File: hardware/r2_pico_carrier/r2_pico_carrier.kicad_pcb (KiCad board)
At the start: 2 copper layers, 80 x 90 mm, 67 parts, among them J1 5V in, J2 OLED socket, SW1 display, U1 PCA9517A

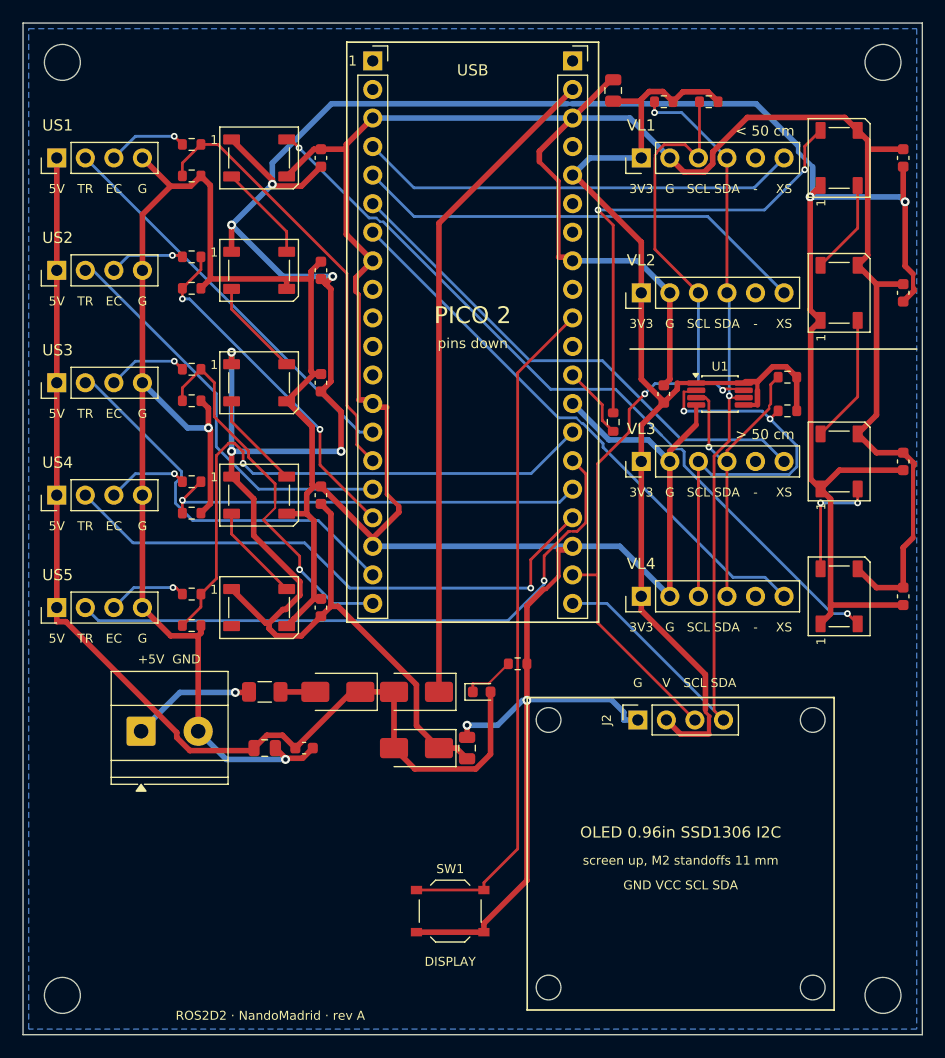
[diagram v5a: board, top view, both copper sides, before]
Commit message: Carrier board: plain 0603 status LEDs, one GPIO each (VL1-4 = GP28/27/22/9, US1-5 = GP0/1/6-8), in place of the WS2812B chain; no VLED rail; BOM 17 lines
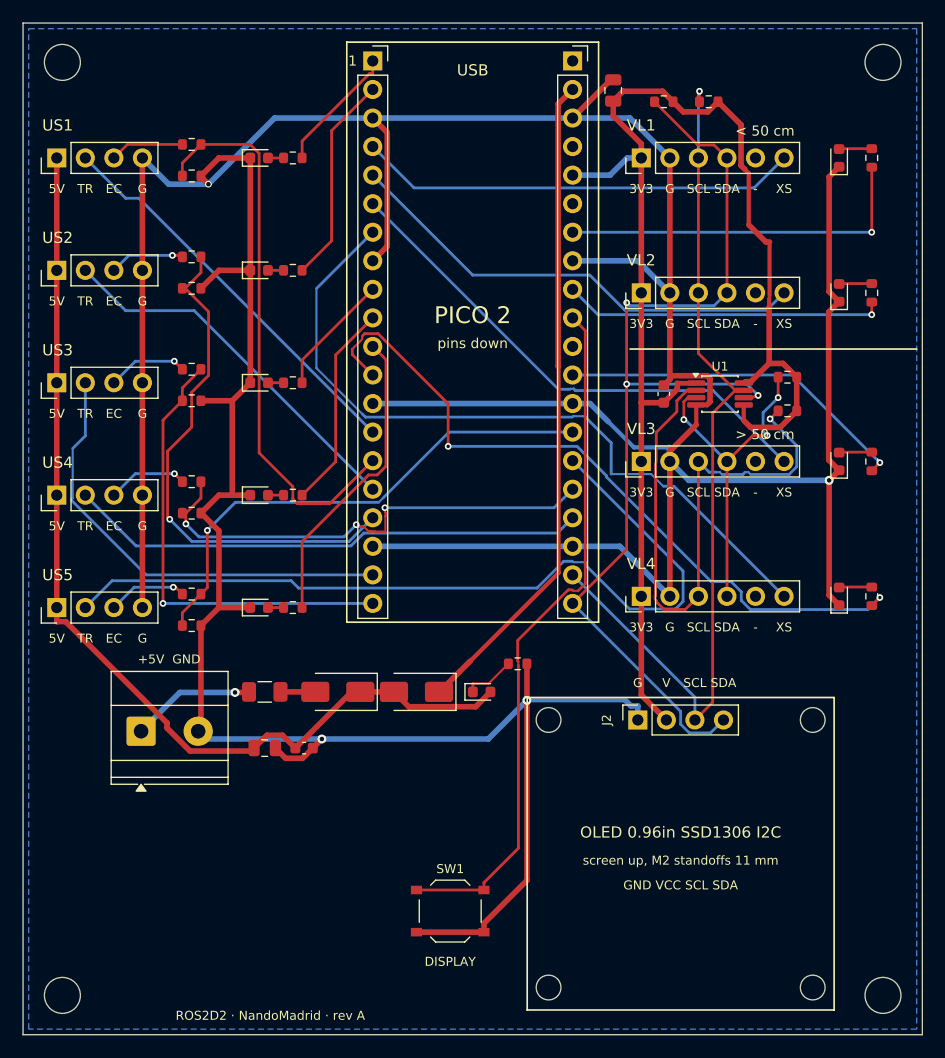
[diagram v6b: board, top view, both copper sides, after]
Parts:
- removed C11, C12, C13, C14, C15, C16, C17, C18, C19: 100n, Capacitor_SMD:C_0603_1608Metric
- removed C3: 10u, Capacitor_SMD:C_0805_2012Metric
- removed D3: SS34, Diode_SMD:D_SMA
- removed R6: 33, Resistor_SMD:R_0603_1608Metric
- added R31: 1k, Resistor_SMD:R_0603_1608Metric, F.Cu at (75.5, 12.0)
- added R32: 1k, Resistor_SMD:R_0603_1608Metric, F.Cu at (75.5, 24.0)
- added R33: 1k, Resistor_SMD:R_0603_1608Metric, F.Cu at (75.5, 39.0)
- added R34: 1k, Resistor_SMD:R_0603_1608Metric, F.Cu at (75.5, 51.0)
- added R35: 1k, Resistor_SMD:R_0603_1608Metric, F.Cu at (24.0, 12.0)
- added R36: 1k, Resistor_SMD:R_0603_1608Metric, F.Cu at (24.0, 22.0)
- added R37: 1k, Resistor_SMD:R_0603_1608Metric, F.Cu at (24.0, 32.0)
- added R38: 1k, Resistor_SMD:R_0603_1608Metric, F.Cu at (24.0, 42.0)
- added R39: 1k, Resistor_SMD:R_0603_1608Metric, F.Cu at (24.0, 52.0)
- LED1, LED2, LED3, LED4, LED5, LED6, LED7, LED8, LED9: value WS2812B -> red; footprint LED_SMD:LED_WS2812B_PLCC4_5.0x5.0mm_P3.2mm -> LED_SMD:LED_0603_1608Metric
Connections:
- JP1 pad 1: unconnected-(JP1-Pin_1-Pad1) -> STAT5
- JP1 pad 10: unconnected-(JP1-Pin_10-Pad10) -> STAT8
- JP1 pad 11: unconnected-(JP1-Pin_11-Pad11) -> STAT9
- JP1 pad 12: unconnected-(JP1-Pin_12-Pad12) -> STAT4
- JP1 pad 2: unconnected-(JP1-Pin_2-Pad2) -> STAT6
- JP1 pad 9: unconnected-(JP1-Pin_9-Pad9) -> STAT7
- JP2 pad 12: LED_DIN_P -> STAT3
- JP2 pad 7: unconnected-(JP2-Pin_7-Pad7) -> STAT1
- JP2 pad 9: unconnected-(JP2-Pin_9-Pad9) -> STAT2
- LED1 pad 1: VLED -> GND
- LED1 pad 2: LED_D1 -> STAT1_A
- LED2 pad 1: VLED -> GND
- LED2 pad 2: LED_D2 -> STAT2_A
- LED3 pad 1: VLED -> GND
- LED3 pad 2: LED_D3 -> STAT3_A
- LED4 pad 1: VLED -> GND
- LED4 pad 2: LED_D4 -> STAT4_A
- LED5 pad 1: VLED -> GND
- LED5 pad 2: LED_D5 -> STAT5_A
- LED6 pad 1: VLED -> GND
- LED6 pad 2: LED_D6 -> STAT6_A
- LED7 pad 1: VLED -> GND
- LED7 pad 2: LED_D7 -> STAT7_A
- LED8 pad 1: VLED -> GND
- LED8 pad 2: LED_D8 -> STAT8_A
- LED9 pad 1: VLED -> GND
- LED9 pad 2: unconnected-(LED9-DOUT-Pad2) -> STAT9_A
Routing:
- net VLED: track 261.3 -> 0.00 mm, vias 8 -> 0
- net LED_D4: track 69.4 -> 0.00 mm, vias 2 -> 0
- net STAT4: track 0.00 -> 65.1 mm, vias 0 -> 2
- net LED_DIN: track 42.6 -> 0.00 mm, vias 2 -> 0
- net GND: track 473.4 -> 431.8 mm
- net STAT1: track 0.00 -> 32.4 mm, vias 0 -> 1
- net STAT3: track 0.00 -> 31.6 mm, vias 0 -> 1
- net STAT2: track 0.00 -> 28.7 mm, vias 0 -> 1
- net STAT9: track 0.00 -> 27.3 mm
- net STAT6: track 0.00 -> 18.7 mm
- net STAT8: track 0.00 -> 18.4 mm
- net +3V3: track 103.7 -> 121.8 mm
- net TRIG5: track 56.1 -> 74.2 mm, vias 1 -> 0
- net XSHUT4: track 50.2 -> 65.9 mm
- net ECHO2_P: track 31.3 -> 46.4 mm, vias 2 -> 1
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
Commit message: Carrier board: USB-C power input (5.1k on CC, own SS34, shared fuse), Qwiic + 6-pin expansion header (I2C, 5V, 3V3, RUN), Astromech logo on the front
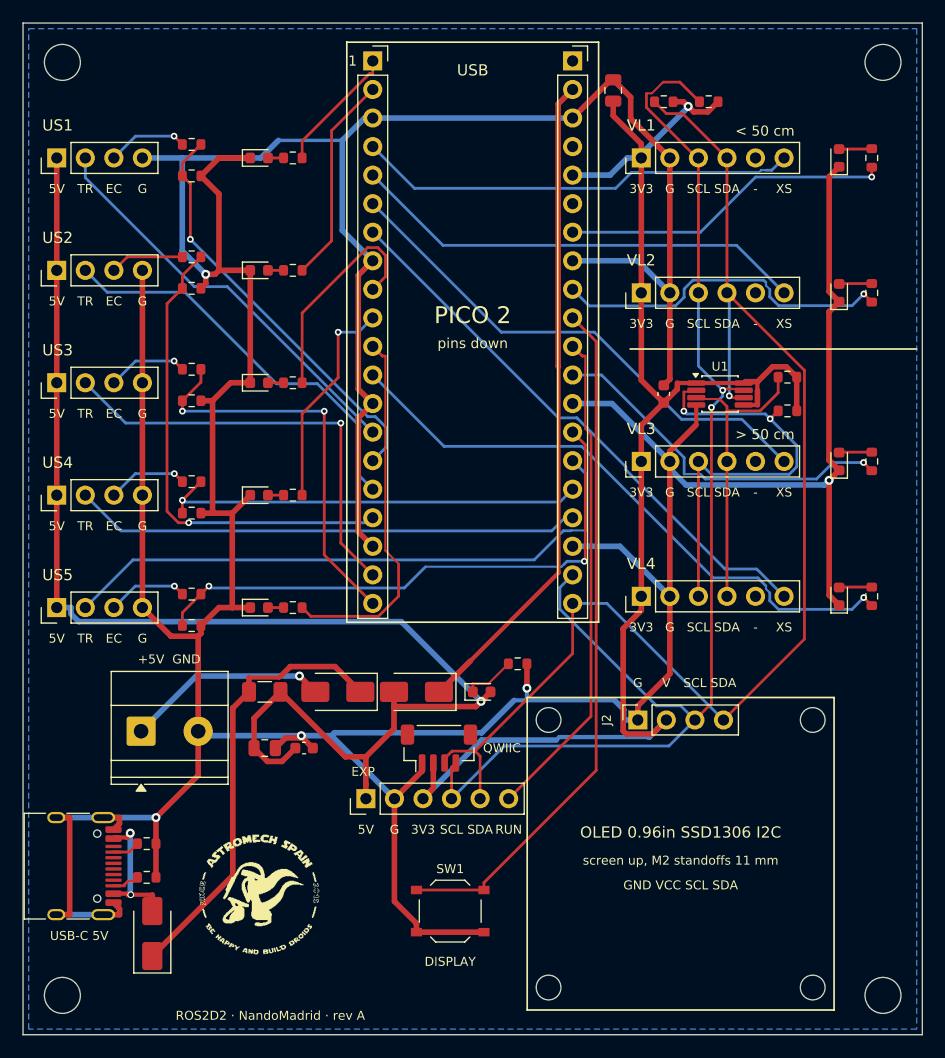
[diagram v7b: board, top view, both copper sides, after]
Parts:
- added D5: SS34, Diode_SMD:D_SMA, F.Cu at (11.5, 81.0)
- added J3: Qwiic, Connector_JST:JST_SH_BM04B-SRSS-TB_1x04-1MP_P1.00mm_Vertical, F.Cu at (37.0, 64.5)
- added J4: expansion, Connector_PinHeader_2.54mm:PinHeader_1x06_P2.54mm_Vertical, F.Cu at (30.5, 69.0)
- added J5: USB-C 5V in, Connector_USB:USB_C_Receptacle_HRO_TYPE-C-31-M-12, F.Cu at (4.00, 75.0)
- added R6: 5.1k, Resistor_SMD:R_0603_1608Metric, F.Cu at (11.0, 73.0)
- added R7: 5.1k, Resistor_SMD:R_0603_1608Metric, F.Cu at (11.0, 76.0)
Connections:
- D1 pad 1: +5V -> 5V_OR
- D1 pad 2: 5V_FUSED -> 5V_IN
- F1 pad 1: 5V_IN -> 5V_OR
- F1 pad 2: 5V_FUSED -> +5V
- JP2 pad 11: unconnected-(JP2-Pin_11-Pad11) -> RUN
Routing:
- net GND: track 431.8 -> 476.0 mm, vias 4 -> 5
- net RUN: track 0.00 -> 44.1 mm
- net 5V_OR: track 0.00 -> 39.6 mm
- net SCL: track 77.9 -> 115.0 mm, vias 1 -> 2
- net +5V: track 89.1 -> 121.8 mm, vias 0 -> 1
- net SDA: track 91.6 -> 117.2 mm, vias 3 -> 1
- net TRIG5: track 74.2 -> 54.0 mm
- net XSHUT4: track 65.9 -> 50.2 mm
- net SCL_L: track 53.3 -> 38.6 mm, vias 1 -> 2
- net ECHO1_P: track 49.8 -> 37.2 mm, vias 0 -> 1
- net VBUS_C: track 0.00 -> 12.3 mm, vias 0 -> 2
- net STAT4: track 65.1 -> 54.3 mm, vias 2 -> 1
- net STAT7: track 10.9 -> 19.8 mm
- net +3V3: track 121.8 -> 130.1 mm, vias 0 -> 1
- net 5V_IN: track 11.0 -> 18.1 mm
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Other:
- board text added: "EXP"
- board text added: "QWIIC"
- board text added: "RUN"
- board text added: "USB-C 5V"

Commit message: Carrier board: J2 is a factory-fitted male header (same part as US1-5); the OLED is soldered on top, flat on the header plastic, instead of plugging into a socket 11 mm up
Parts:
- J2: value OLED socket -> OLED header; footprint Connector_PinSocket_2.54mm:PinSocket_1x04_P2.54mm_Vertical -> Connector_PinHeader_2.54mm:PinHeader_1x04_P2.54mm_Vertical
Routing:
- net +5V: track 121.8 -> 100.2 mm
- net XSHUT4: track 50.2 -> 69.0 mm, vias 0 -> 2
- net SCL: track 115.0 -> 103.7 mm, vias 2 -> 3
- net SCL_L: track 38.6 -> 28.8 mm, vias 2 -> 3
- net GND: track 476.0 -> 483.0 mm, vias 5 -> 3
- net XSHUT3: track 46.1 -> 52.7 mm
- net STAT9: track 33.0 -> 27.3 mm
- net STAT7: track 19.8 -> 14.6 mm, vias 0 -> 1
- net ECHO5_P: track 50.9 -> 46.3 mm
- net +3V3: track 130.1 -> 125.5 mm, vias 1 -> 0
- net ECHO1_P: track 37.2 -> 40.5 mm, vias 1 -> 0
- net STAT1: track 29.5 -> 32.4 mm
- net TRIG2: track 36.3 -> 33.6 mm
- net ECHO3_P: track 35.9 -> 38.1 mm, vias 2 -> 1
- net STAT3: track 32.2 -> 30.1 mm
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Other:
- board text added: "screen up, soldered on J2"
- board text removed: "screen up, M2 standoffs 11 mm"
